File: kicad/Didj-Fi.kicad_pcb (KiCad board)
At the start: 2 copper layers, 44.9 x 33.5 mm, 20 parts, among them J1 didj_cart, J3 USB_B_Micro, U1 CH340E, U2 ESP-12F

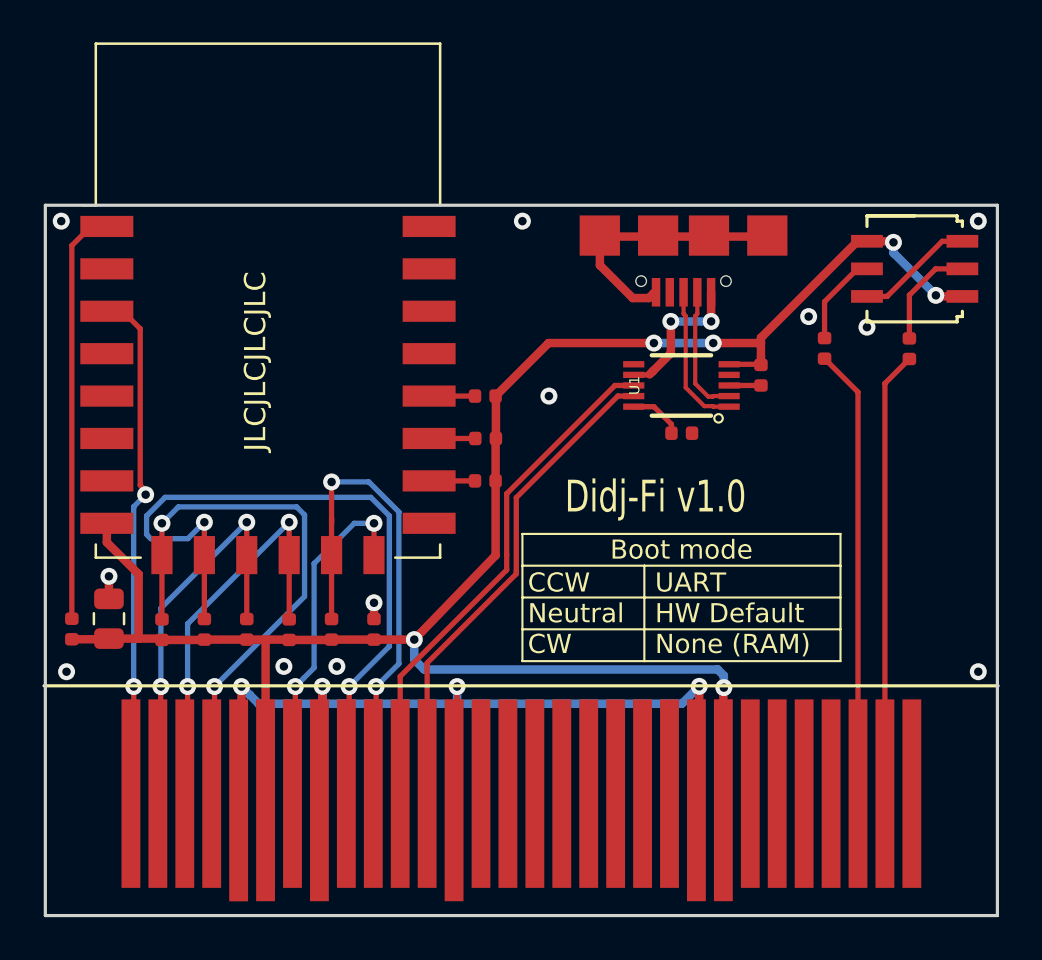
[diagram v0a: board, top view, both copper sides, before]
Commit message: Modified project to act as a blank slate
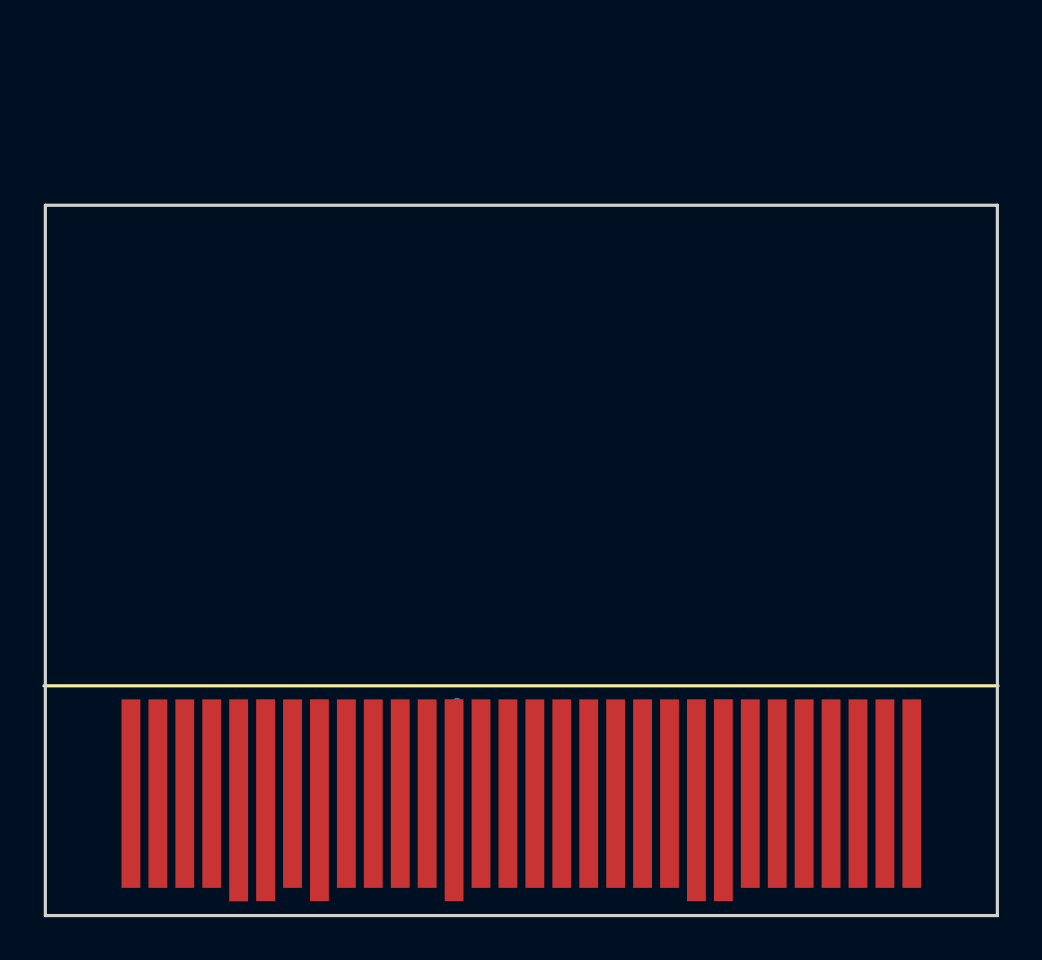
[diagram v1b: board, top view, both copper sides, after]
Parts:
- removed C1, C2, C4: 0.1u, Capacitor_SMD:C_0402_1005Metric
- removed C3: 22u, Capacitor_SMD:C_0805_2012Metric
- removed J3: USB_B_Micro, project:C40942
- removed R1, R11, R3, R4, R5, R7, R8, R9: 10k, Resistor_SMD:R_0402_1005Metric
- removed R10, R2: 4.7k, Resistor_SMD:R_0402_1005Metric
- removed R6: 3k, Resistor_SMD:R_0402_1005Metric
- removed S1: CS-4-22YA, project:cs-4
- removed U1: CH340E, project:MSOP10
- removed U2: ESP-12F, RF_Module:ESP-12E
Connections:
- J1 pad 1: /EN -> unconnected-(J1C-GPIO-Pad1)
- J1 pad 10: /DAT1 -> unconnected-(J1C-DAT1-Pad10)
- J1 pad 11: /RX -> unconnected-(J1B-RX-Pad11)
- J1 pad 12: /TX -> unconnected-(J1B-TX-Pad12)
- J1 pad 13: GND -> unconnected-(J1B-GND-Pad13)
- J1 pad 14: Net-(J1-Pad14) -> unconnected-(J1A-D0-Pad14)
- J1 pad 15: Net-(J1-Pad15) -> unconnected-(J1A-D1-Pad15)
- J1 pad 16: Net-(J1-Pad16) -> unconnected-(J1A-D2-Pad16)
- J1 pad 17: Net-(J1-Pad17) -> unconnected-(J1A-D3-Pad17)
- J1 pad 18: Net-(J1-Pad18) -> unconnected-(J1A-~{WP}-Pad18)
- J1 pad 19: Net-(J1-Pad19) -> unconnected-(J1A-~{WE}-Pad19)
- J1 pad 2: /DAT2 -> unconnected-(J1C-DAT2-Pad2)
- J1 pad 20: Net-(J1-Pad20) -> unconnected-(J1A-ALE-Pad20)
- J1 pad 21: Net-(J1-Pad21) -> unconnected-(J1A-CLE-Pad21)
- J1 pad 22: GND -> unconnected-(J1A-GND-Pad22)
- J1 pad 23: +3V3 -> unconnected-(J1A-VCC-Pad23)
- J1 pad 24: Net-(J1-Pad24) -> unconnected-(J1A-~{CE}-Pad24)
- J1 pad 25: Net-(J1-Pad25) -> unconnected-(J1A-~{RE}-Pad25)
- J1 pad 26: Net-(J1-Pad26) -> unconnected-(J1A-R/~{B}-Pad26)
- J1 pad 27: Net-(J1-Pad27) -> unconnected-(J1A-D4-Pad27)
- J1 pad 28: /D5 -> unconnected-(J1A-D5-Pad28)
- J1 pad 29: /D6 -> unconnected-(J1A-D6-Pad29)
- J1 pad 3: /DAT3 -> unconnected-(J1C-DAT3-Pad3)
- J1 pad 30: Net-(J1-Pad30) -> unconnected-(J1A-D7-Pad30)
- J1 pad 4: /CMD -> unconnected-(J1C-CMD-Pad4)
- J1 pad 5: GND -> unconnected-(J1C-GND-Pad5)
- J1 pad 6: +3V3 -> unconnected-(J1C-VCC-Pad6)
- J1 pad 7: /CLK -> unconnected-(J1C-CLK-Pad7)
- J1 pad 8: GND -> unconnected-(J1C-GND-Pad8)
- J1 pad 9: /DAT0 -> unconnected-(J1C-DAT0-Pad9)
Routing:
- net +3V3: track 93.2 -> 0.00 mm, vias 6 -> 0
- net GND: track 65.7 -> 0.00 mm, vias 16 -> 0
- net /DAT0: track 34.6 -> 0.00 mm, vias 2 -> 0
- net /CMD: track 26.6 -> 0.00 mm, vias 2 -> 0
- net /RX: track 24.3 -> 0.00 mm
- net /DAT1: track 24.2 -> 0.00 mm, vias 2 -> 0
- net /EN: track 24.2 -> 0.00 mm, vias 2 -> 0
- net /TX: track 23.2 -> 0.00 mm
- net /D5: track 21.2 -> 0.00 mm
- net /D6: track 21.0 -> 0.00 mm
- net /~RST: track 19.6 -> 0.00 mm
- net /DAT3: track 19.4 -> 0.00 mm, vias 2 -> 0
- net /DAT2: track 19.0 -> 0.00 mm, vias 2 -> 0
- net /CLK: track 16.3 -> 0.00 mm, vias 2 -> 0
- net VBUS: track 7.05 -> 0.00 mm, vias 2 -> 0
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- added copper zone on B.Cu, net unconnected-(J1C-GND-Pad5)
- added copper zone on F.Cu, net unconnected-(J1C-GND-Pad5)
- removed copper zone on B.Cu, net GND
- removed copper zone on F.Cu, net GND
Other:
- net class Default removed
- net class Power removed
- board text removed: "Boot mode"
- board text removed: "CCW Neutral CW"
- board text removed: "Didj-Fi v1.0"
- board text removed: "JLCJLCJLCJLC"
- board text removed: "UART HW Default None (RAM)"
- board text removed: "jkent.net/w/didjfi"
